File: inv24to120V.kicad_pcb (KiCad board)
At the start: 2 copper layers, 237.5 x 150 mm, 164 parts, among them IC1 MCP2551-E_SN, IC2 ISO7221AQDRQ1, J1 70543-0003, J12 BR-120, J2 70543-0001, J3 70543-0001, J4 Screw_Terminal_01x03, J5 BR-120, Q1 IRFZ44NPBF, Q2 IRFZ44NPBF, Q3 ZXTN2010ZTA, Q4 ZXTN2010ZTA, Q5 ZXTP2012ZTA, Q6 ZXTP2012ZTA, Q7 SUP53P06-20-E3, Q8 STGIF7CH60TS-L, SW1 SW_DIP_x02, U1 ESP32-DEVKITC-32D, U15 FOD817A3SD, U2 LM2576D2T-15G, U3 LM2576-3.3WU, U4 LM2576D2TR4-5G, U5 FOD817A3SD

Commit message: add pause cause mati argue
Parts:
- added C24: 220uF/50V, Capacitor_SMD:CP_Elec_16x17.5, F.Cu at (89.2, 56.5)
- added C25: 220uF/50V, Capacitor_SMD:CP_Elec_16x17.5, F.Cu at (57.0, 113.2)
- added D6: BYV29X-600, Package_TO_SOT_THT:TO-220-2_Horizontal_TabUp, B.Cu at (98.7, 102.5)
- D8: footprint mod:TO507P1020X460X2000-2 -> Package_TO_SOT_THT:TO-220-2_Horizontal_TabUp; moved to B.Cu
- F3, F4, F5: footprint Fuse:Fuse_2920_7451Metric_Pad2.10x5.45mm_HandSolder -> Fuse:Fuse_2512_6332Metric_Pad1.52x3.35mm_HandSolder
- Q7: footprint mod:TO254P465X1028X1931-3P -> Package_TO_SOT_THT:TO-220-3_Horizontal_TabUp; moved to B.Cu
- moved C6 206.9 mm to (175.2, 30.0)
- moved Z1 194.7 mm to (211.2, 144.5)
- moved Q7 191.1 mm to (203.3, 139.5), turned to -90 degrees
- moved BC19 184.7 mm to (212.2, 152.5)
- moved BC14 176.1 mm to (205.8, 152.5)
- moved R40 175.0 mm to (243.0, 74.0), turned to 180 degrees
- moved BC11 166.0 mm to (55.0, 129.0), turned to 180 degrees
- moved C2 154.7 mm to (131.5, 31.5)
- moved BC13 146.9 mm to (94.2, 130.0), turned to 180 degrees
- moved R35 146.1 mm to (54.0, 126.0)
- moved BC16 140.9 mm to (211.5, 114.5), turned to 180 degrees
- moved R46 134.6 mm to (100.0, 45.2)
- moved D3 130.8 mm to (62.0, 146.0), turned to 180 degrees
- moved R45 130.1 mm to (212.5, 70.5), turned to -90 degrees
- moved RT1 128.3 mm to (213.0, 131.6), turned to 180 degrees
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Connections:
- BC18 pad 1: +5V -> Net-(PS1-+VIN_)
- BC18 pad 2: GND -> Net-(PS1--VIN)
- BC23 pad 2: GND2 -> GND
- BC7 pad 2: GND2 -> GND
- BX2 pad 1: Net-(BX2-Pad1) -> +5V
- BX2 pad 2: +5V -> Net-(PS1-+VIN_)
- BX4 pad 1: Net-(BX4-Pad1) -> GND
- BX4 pad 2: GND -> Net-(PS1--VIN)
- C11 pad 2: GND2 -> GND
- C16 pad 2: GND2 -> GND
- C18 pad 1: +5V -> Net-(PS1-+VIN_)
- C18 pad 2: GND -> Net-(PS1--VIN)
- C3 pad 1: Net-(BX2-Pad1) -> +5V
- C3 pad 2: Net-(BX4-Pad1) -> GND
- C6 pad 2: GND2 -> GND
- PS1 pad 1: GND -> Net-(PS1--VIN)
- PS1 pad 3: +5V -> Net-(PS1-+VIN_)
- Q8 pad 24: V_DC_LINK -> VBUS
- U1 pad J2-1: +3.3V -> unconnected-(U1-3V3-PadJ2-1)
- U1 pad J2-6: ANALOG_CMD -> TEMPERATURE_IPM
- U1 pad J2-7: TEMPERATURE_IPM -> T2
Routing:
- net GND: track 0.00 -> 709.5 mm, vias 0 -> 18
- net Earth: track 0.00 -> 648.2 mm
- net +24V: track 0.00 -> 508.9 mm, vias 0 -> 4
- net +3.3V: track 0.00 -> 395.9 mm, vias 0 -> 12
- net +5V: track 0.00 -> 278.9 mm, vias 0 -> 2
- net DIN_A: track 0.00 -> 264.3 mm, vias 0 -> 6
- net DIN_B: track 0.00 -> 256.5 mm, vias 0 -> 6
- net GNDPWR: track 0.00 -> 207.1 mm, vias 0 -> 1
- net Net-(D10-K): track 0.00 -> 206.5 mm, vias 0 -> 2
- net CIN: track 0.00 -> 197.4 mm
- net TEMPERATURE_IPM: track 0.00 -> 174.6 mm, vias 0 -> 2
- net T2: track 0.00 -> 170.0 mm, vias 0 -> 1
- net PWM0_L: track 0.00 -> 156.5 mm, vias 0 -> 1
- net PWM1_L: track 0.00 -> 156.2 mm, vias 0 -> 1
- net PWM2_L: track 0.00 -> 154.4 mm
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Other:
- board size 237.5 x 150 mm -> 227 x 150 mm
- board text added: "+24V"
- board text added: "GND"

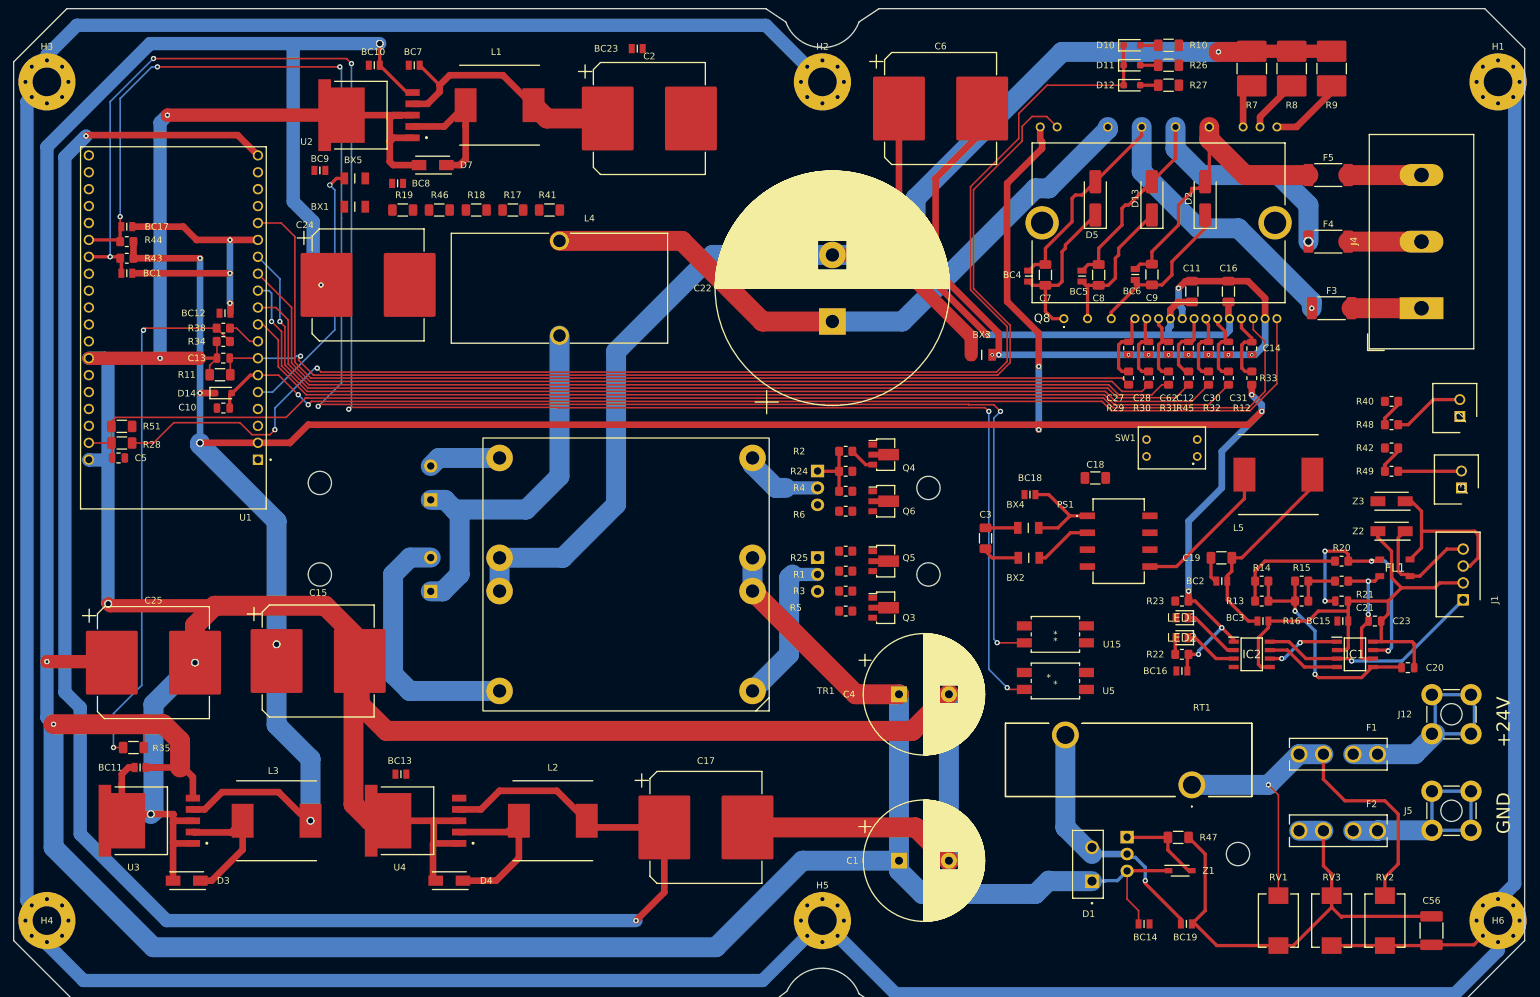
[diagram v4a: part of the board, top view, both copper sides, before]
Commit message: finish routing next add copper for power
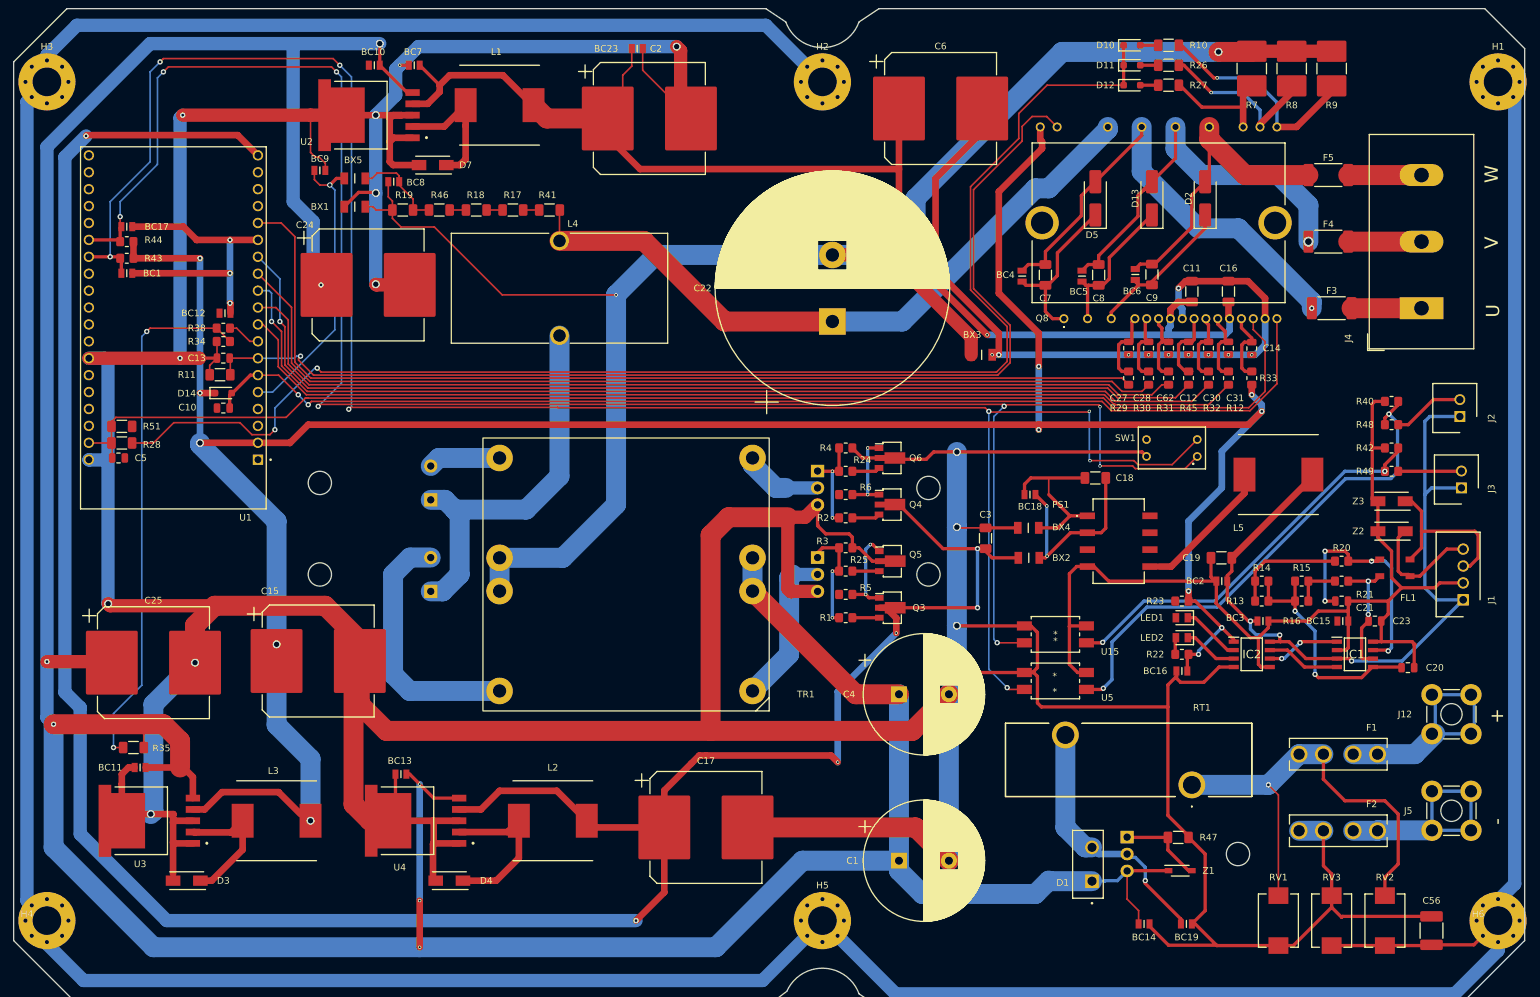
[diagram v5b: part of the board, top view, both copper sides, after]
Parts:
- moved R2 10.0 mm to (161.0, 91.5)
- moved Q4 7.56 mm to (167.9, 89.5)
- moved R1 7.00 mm to (161.0, 106.5)
- moved Q6 6.57 mm to (167.9, 82.5)
- moved R3 6.50 mm to (161.0, 96.0)
- moved R4 6.50 mm to (161.0, 81.0)
- moved R25 3.00 mm to (161.0, 99.5)
- moved R5 2.50 mm to (161.0, 103.0)
- moved R6 2.50 mm to (161.0, 88.0)
- moved BC4 1.00 mm to (187.5, 55.2)
- moved Q3 1.00 mm to (168.0, 105.0)
- moved Q5 1.00 mm to (168.0, 98.0)
- moved BC8 0.63 mm to (93.1, 41.0), turned to 180 degrees
- turned BC18 to 180 degrees
- turned R18 to 0 degrees
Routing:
- net GND: track 709.5 -> 1107.3 mm, vias 18 -> 27
- net +5V: track 278.9 -> 383.7 mm, vias 2 -> 6
- net GND1: track 79.4 -> 158.6 mm
- net Net-(R40-Pad1): track 4.33 -> 77.1 mm, vias 0 -> 2
- net +15V: track 126.7 -> 187.2 mm
- net Net-(R42-Pad1): track 4.33 -> 59.8 mm, vias 0 -> 2
- net GNDPWR: track 207.1 -> 260.5 mm, vias 1 -> 2
- net +5P: track 64.9 -> 114.0 mm, vias 1 -> 3
- net DIN_B: track 256.5 -> 294.7 mm, vias 6 -> 8
- net DIN_A: track 264.3 -> 302.1 mm, vias 6 -> 8
- net +24V: track 508.9 -> 542.8 mm, vias 4 -> 7
- net Net-(Q8-NW): track 11.3 -> 33.3 mm, vias 0 -> 1
- net Net-(PS1-+VIN_): track 8.79 -> 29.3 mm, vias 0 -> 2
- net Net-(Q8-NV): track 8.20 -> 25.7 mm, vias 0 -> 1
- net Net-(PS1--VIN): track 14.6 -> 31.5 mm
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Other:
- board text added: "+"
- board text added: "-"
- board text added: "U"
- board text added: "V"
- board text added: "W"
- board text removed: "+24V"
- board text removed: "GND"

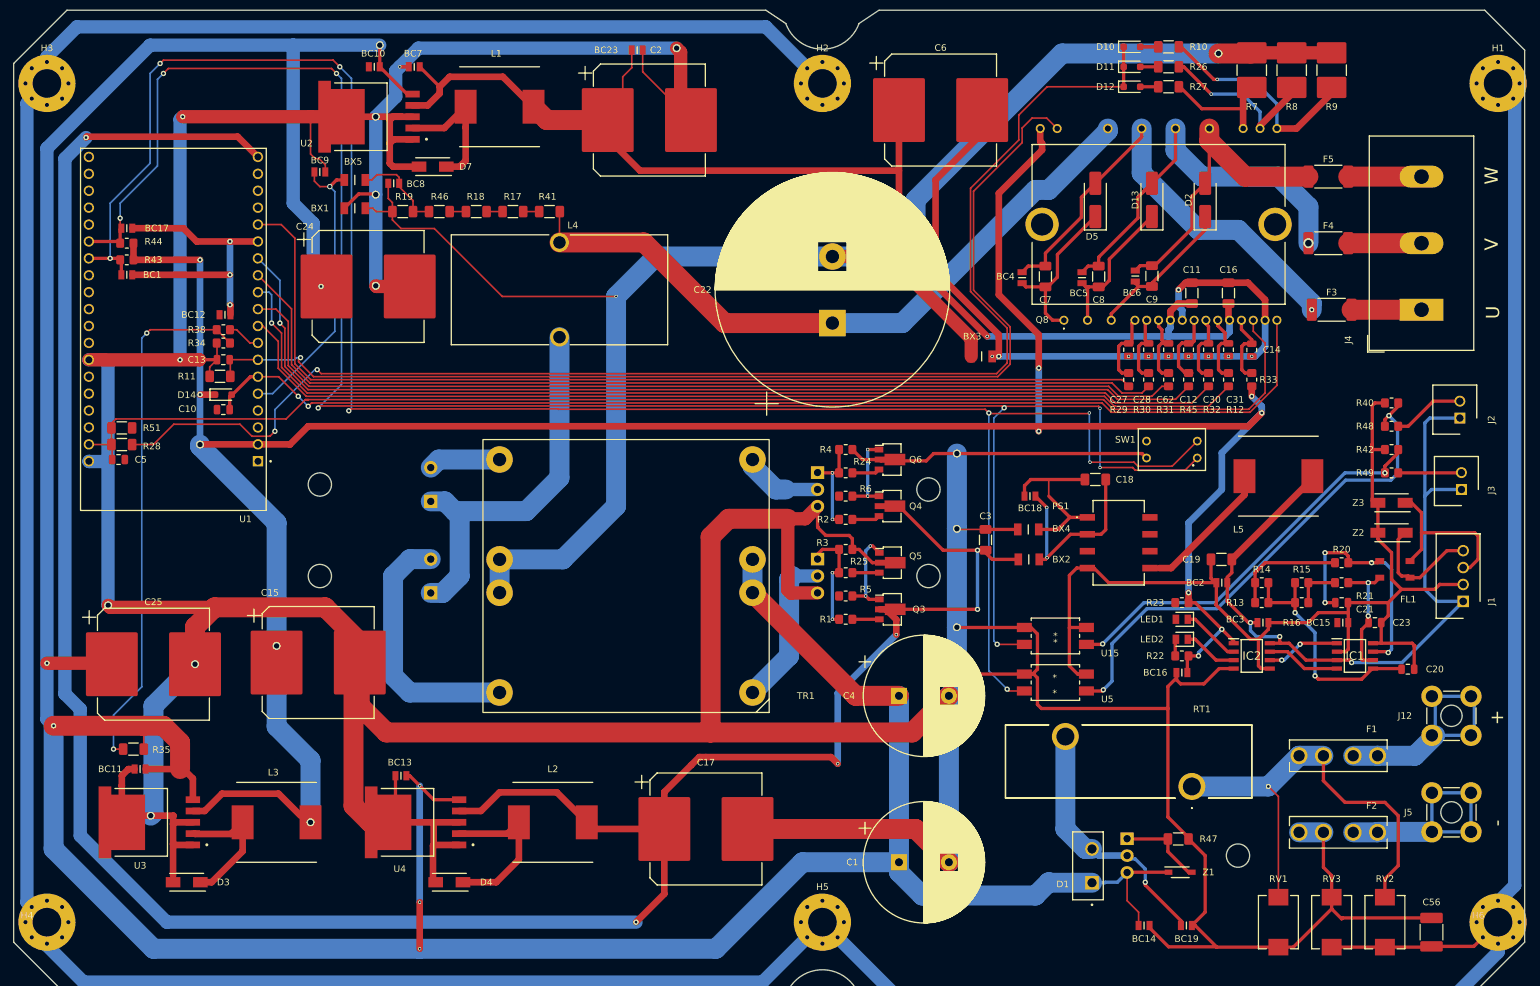
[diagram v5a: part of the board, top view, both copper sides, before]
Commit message: renumber ref and schematic 적용
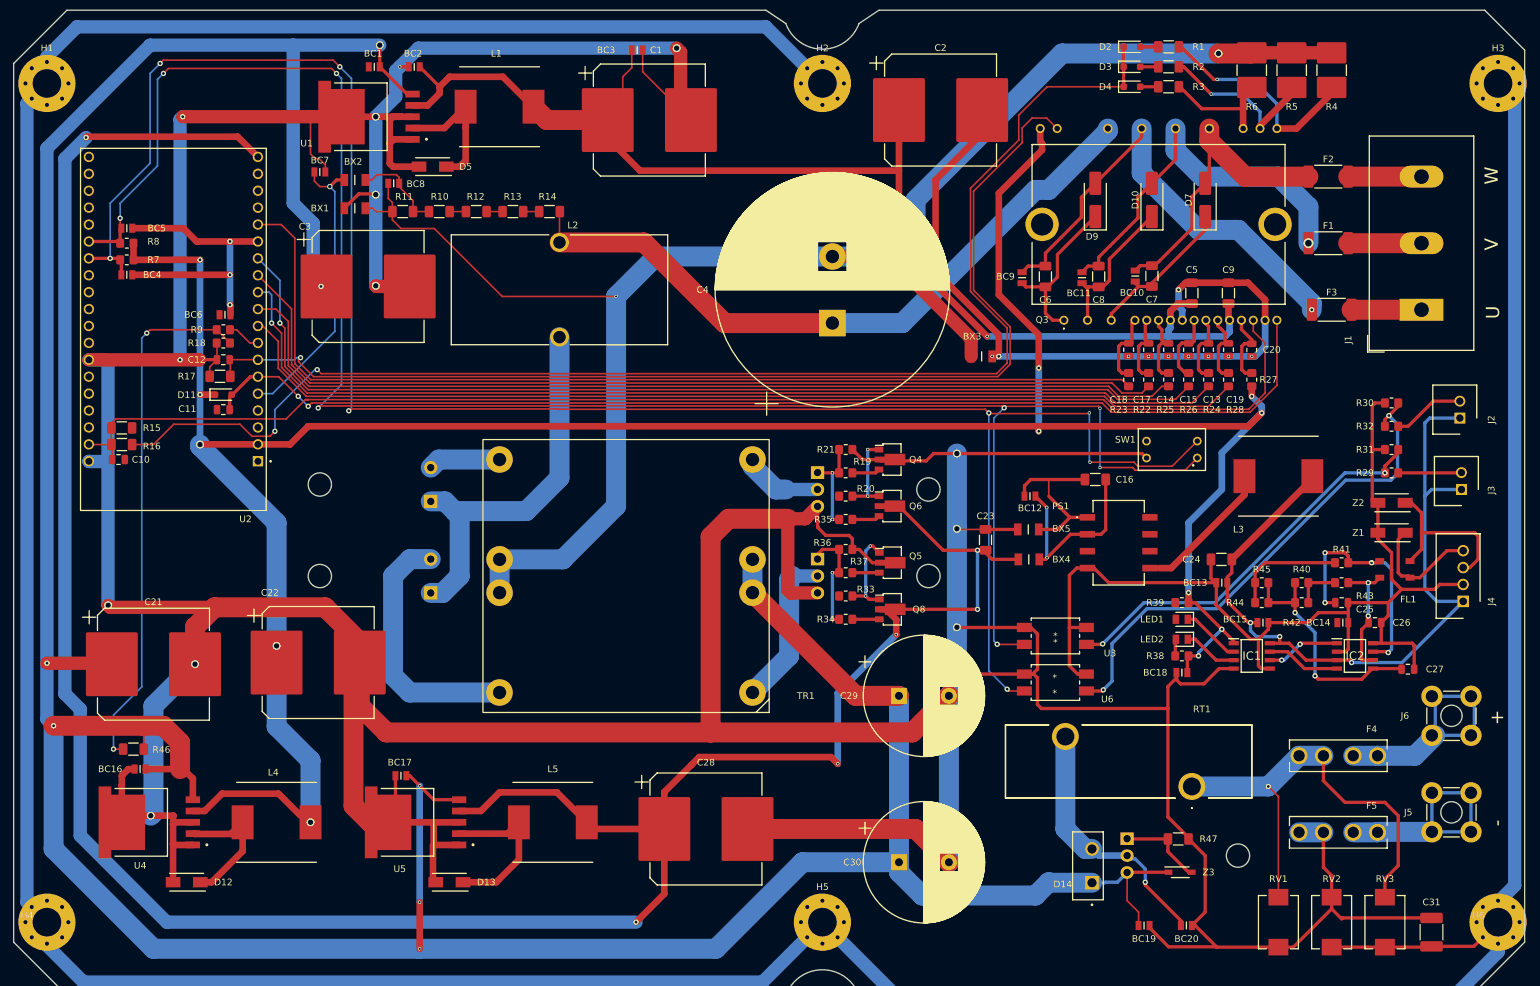
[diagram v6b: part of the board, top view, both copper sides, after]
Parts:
- renumbered BC10 to BC1, BC6 to BC10, BC5 to BC11, BC18 to BC12, BC2 to BC13, BC15 to BC14, BC3 to BC15, BC11 to BC16, BC13 to BC17, BC16 to BC18, BC14 to BC19, BC7 to BC2, BC19 to BC20, BC23 to BC3, BC1 to BC4, BC17 to BC5, BC12 to BC6, BC9 to BC7, BC4 to BC9, BX5 to BX2, BX2 to BX4, BX4 to BX5, C2 to C1, C5 to C10, C10 to C11, C13 to C12, C30 to C13, C62 to C14, C12 to C15, C18 to C16, C28 to C17, C27 to C18, C31 to C19, C6 to C2, C14 to C20, C25 to C21, C15 to C22, C3 to C23, C19 to C24, C21 to C25, C23 to C26, C20 to C27, C17 to C28, C4 to C29, C24 to C3, C1 to C30, C56 to C31, C22 to C4, C11 to C5, C7 to C6, C9 to C7, C16 to C9, D13 to D10, D14 to D11, D3 to D12, D4 to D13, D1 to D14, D10 to D2, D11 to D3, D12 to D4, D7 to D5, D2 to D7, D5 to D9, F4 to F1, F5 to F2, F1 to F4, F2 to F5, H3 to H1, H1 to H3, IC2 to IC1, IC1 to IC2, J4 to J1, J1 to J4, J12 to J6, L4 to L2, L5 to L3, L3 to L4, L2 to L5, Q8 to Q3, Q6 to Q4, Q4 to Q6, Q3 to Q8, R10 to R1, R46 to R10, R19 to R11, R18 to R12, R17 to R13, R41 to R14, R51 to R15, R28 to R16, R11 to R17, R34 to R18, R24 to R19, R26 to R2, R6 to R20, R4 to R21, R30 to R22, R29 to R23, R32 to R24, R31 to R25, R45 to R26, R33 to R27, R12 to R28, R49 to R29, R27 to R3, R40 to R30, R42 to R31, R48 to R32, R5 to R33, R1 to R34, R2 to R35, R3 to R36, R25 to R37, R22 to R38, R23 to R39, R9 to R4, R15 to R40, R20 to R41, R16 to R42, R21 to R43, R13 to R44, R14 to R45, R35 to R46, R8 to R5, R7 to R6, R43 to R7, R44 to R8, R38 to R9, RV3 to RV2, RV2 to RV3, U2 to U1, U1 to U2, U15 to U3, U3 to U4, U4 to U5, U5 to U6, Z2 to Z1, Z3 to Z2, Z1 to Z3

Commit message: check DRC
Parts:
- added x: via_power_out, mod:via_power_out, F.Cu at (231.4, 46.8)
- added x: via_power_out, mod:via_power_out, F.Cu at (227.1, 56.1)
- moved F2 1.12 mm to (234.0, 39.0)
- moved C5 1.03 mm to (213.2, 56.5)
- moved C9 1.03 mm to (218.8, 56.5)
- moved F1 0.50 mm to (234.0, 50.0)
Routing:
- net GND: track 1107.3 -> 1131.8 mm, vias 27 -> 28
- net Net-(D6-K): track 58.6 -> 76.7 mm
- net Net-(F1-Pad2_1): track 69.2 -> 58.6 mm, vias 1 -> 3
- net +5P: track 114.0 -> 123.6 mm
- net +5V: track 383.7 -> 376.6 mm
- net +15V: track 187.2 -> 191.3 mm
- net VDC_IN: track 5.02 -> 7.92 mm
- net T2: track 170.0 -> 172.1 mm
- net Net-(D10-K): track 206.5 -> 208.3 mm
- net +3.3V: track 397.0 -> 395.2 mm
- net PHASE_U: track 71.9 -> 73.3 mm
- net VBOOT_U: track 24.8 -> 23.8 mm
- net PHASE_V: track 62.3 -> 63.1 mm
- net GNDPWR: track 260.5 -> 259.9 mm
- net DIN_A: track 302.1 -> 302.7 mm
- added copper zone on B.Cu, net +24V
- added copper zone on F.Cu, net +24V
- added copper zone on B.Cu, net GND
- added copper zone on F.Cu, net GND
- added copper zone on B.Cu, net GND1
- added copper zone on F.Cu, net GND1
- added copper zone on B.Cu, net Net-(D1-A)
- added copper zone on B.Cu, net Net-(F1-Pad2_1)
- added copper zone on B.Cu, net Net-(J12-Pin_1)
- added copper zone on B.Cu, net Net-(J5-Pin_1)
- added copper zone on B.Cu, net Net-(Q1-D)
- added copper zone on B.Cu, net Net-(Q2-D)
